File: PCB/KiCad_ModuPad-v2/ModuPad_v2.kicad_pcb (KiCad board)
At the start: 2 copper layers, 105 x 125 mm, 95 parts, among them J1 Conn_01x02, SW1 SW_Push, SW10 SW_Push, SW11 SW_Push, SW12 SW_Push, SW13 SW_Push, SW14 SW_Push, SW15 SW_Push, SW16 SW_Push, SW17 SW_Push, SW18 SW_Push, SW19 SW_Push, SW2 SW_Push, SW20 SW_Push, SW21 SW_Push, SW22 SW_Push, SW23 SW_Push, SW24 SW_Push, SW25 SW_Push, SW26_SPDT1 SW_SPDT, SW27_RST1 SW_Push_45deg, SW3 SW_Push, SW4 SW_Push, SW5 SW_Push, SW6 SW_Push, SW7 SW_Push, SW8 SW_Push, SW9 SW_Push

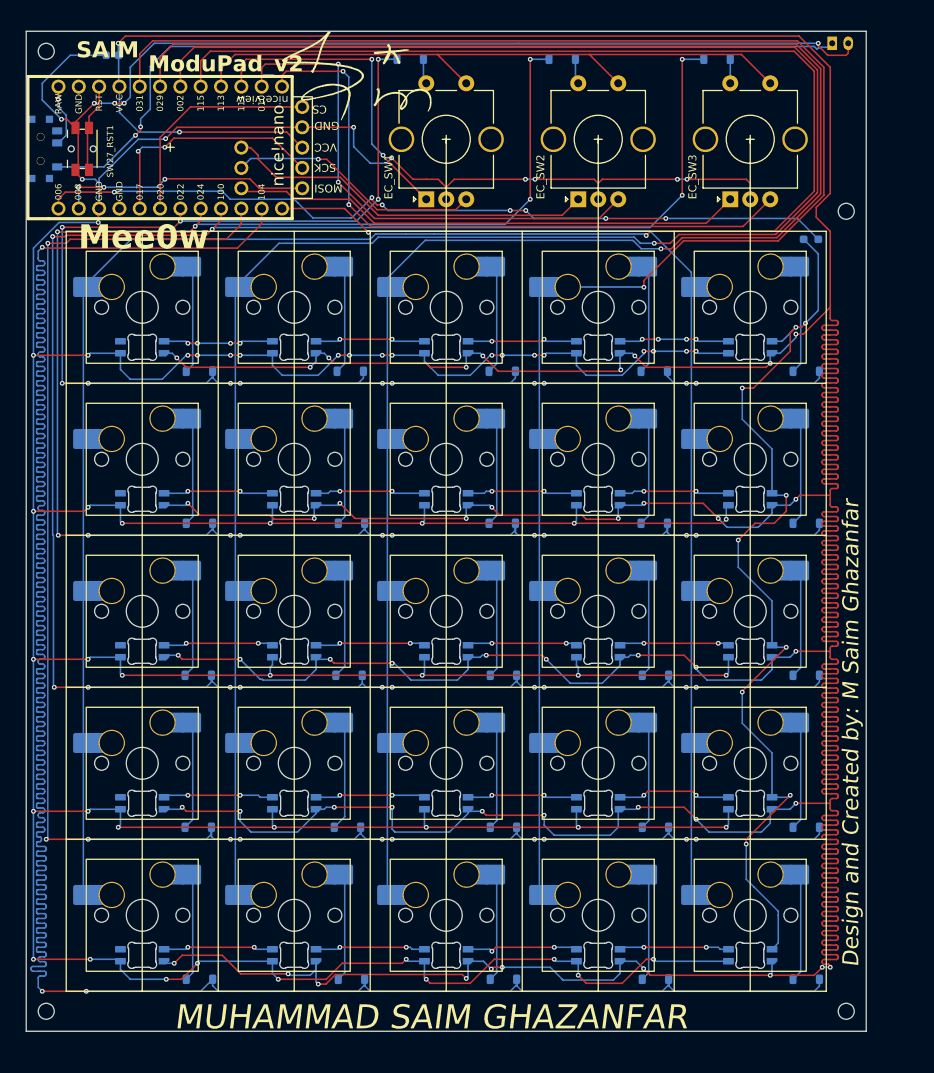
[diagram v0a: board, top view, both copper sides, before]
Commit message: Update BOM and PCB
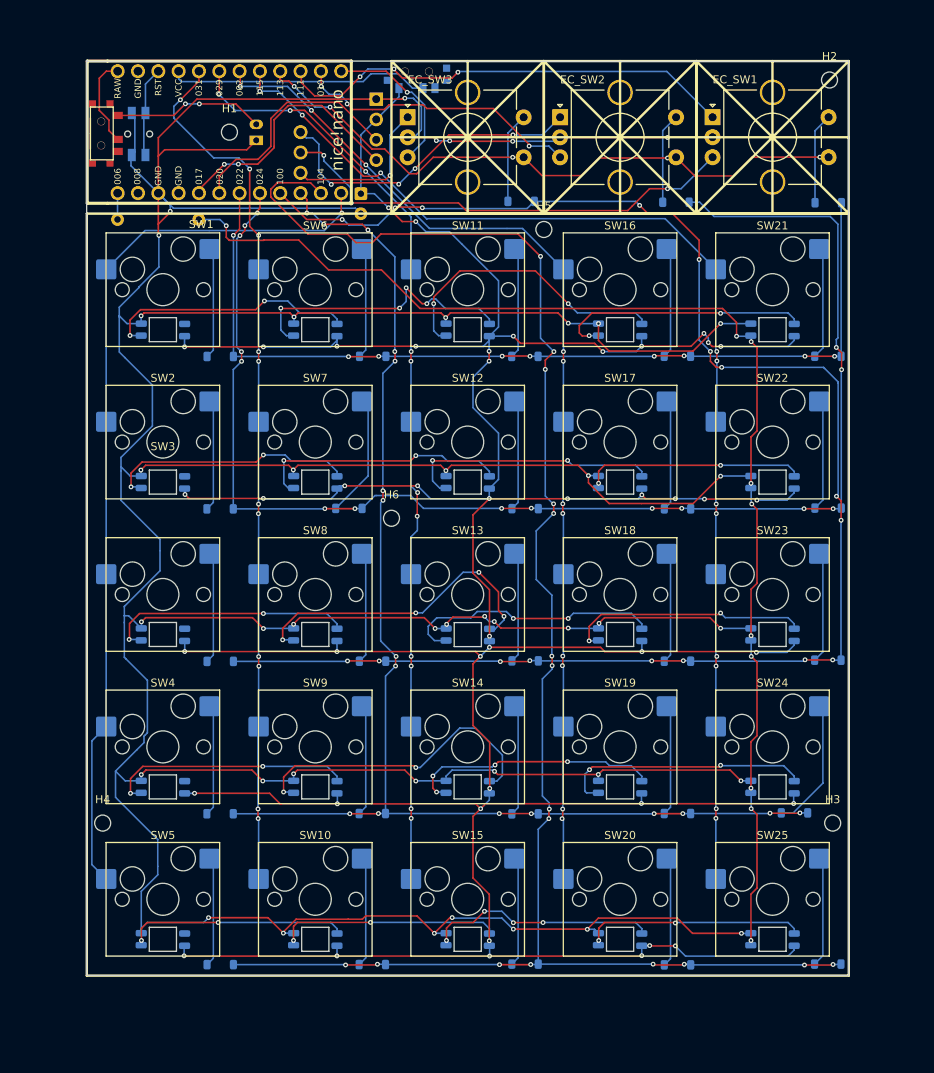
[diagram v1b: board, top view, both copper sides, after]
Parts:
- removed Display1: nice!view, nice!view:nice_view
- removed G*** (x2): LOGO, SAIM's_Signature-Silkscreen:SAIM_Signature_Silkscreen_20x18.4-mm
- removed G***: LOGO, Branding:Flag-orpheus-bw_Branding_HACK-CLUB
- removed REF** (x4): MountingHole_2mm, MountingHole:MountingHole_2mm
- removed SW26_SPDT1: SW_SPDT, Power-Switch-Battery:SPDT_C128955
- added BAT-Power-Switch_SPDT1: SW_SPDT, Power-Switch-Battery:SPDT_C128955, B.Cu at (59.4, 62.8)
- added H1: MountingHole, MountingHole:MountingHole_2mm, F.Cu at (75.4, 62.6)
- added H2: MountingHole, MountingHole:MountingHole_2mm, F.Cu at (150.4, 56.1)
- added H3: MountingHole, MountingHole:MountingHole_2mm, F.Cu at (150.8, 149.0)
- added H4: MountingHole, MountingHole:MountingHole_2mm, F.Cu at (59.6, 149.0)
- added H5: MountingHole, MountingHole:MountingHole_2mm, F.Cu at (114.7, 74.8)
- added H6: MountingHole, MountingHole:MountingHole_2mm, F.Cu at (95.7, 110.9)
- added J2: OLED_128x32, ScottoKeebs_Components:OLED_128x32, F.Cu at (95.3, 68.3)
- added LED-OLED-Power-Switch_SPDT2: SW_SPDT, Power-Switch-Battery:SPDT_C128955, F.Cu at (98.8, 55.0)
- C1: footprint Capacitor_SMD:C_0603_1608Metric -> Capacitor_THT:CP_Radial_D6.3mm_P2.50mm
- D_1, D_10, D_11, D_12, D_13, D_14, D_15, D_16, D_17, D_18, D_19, D_2, D_20, D_21, D_22, D_23, D_24, D_25, D_26, D_27, D_28, D_3, D_4, D_5, D_6, D_7, D_8, D_9: footprint Diode_SMD:D_SOD-123 -> ScottoKeebs_Components:Diode_SOD-123
- LED_1, LED_10, LED_11, LED_12, LED_13, LED_14, LED_15, LED_16, LED_17, LED_18, LED_19, LED_2, LED_20, LED_21, LED_22, LED_23, LED_24, LED_25, LED_3, LED_4, LED_5, LED_6, LED_7, LED_8, LED_9: footprint SK6812MINI-E:SK6812MINI-E -> SK6812MINI-E:LED_SK6812MINI; moved to F.Cu
- R1: footprint Resistor_SMD:R_0603_1608Metric_Pad0.98x0.95mm_HandSolder -> Resistor_THT:R_Axial_DIN0207_L6.3mm_D2.5mm_P10.16mm_Horizontal
- SW1, SW10, SW11, SW12, SW13, SW14, SW15, SW16, SW17, SW18, SW19, SW2, SW20, SW21, SW22, SW23, SW24, SW25, SW3, SW4, SW5, SW6, SW7, SW8, SW9: footprint MX-Style-Cherry-Switches-with-Kilah-HotSwap-Socket:SW_MX_HS_CPG151101S11_1u -> ScottoKeebs_Hotswap:Hotswap_MX_1.00u; moved to F.Cu
- SW27_RST1: moved to B.Cu
- moved R1 86.7 mm to (61.4, 73.5), turned to 0 degrees
- moved SW21 78.8 mm to (143.3, 82.3), turned to 0 degrees
- moved SW22 78.8 mm to (143.3, 101.3), turned to 0 degrees
- moved SW23 78.8 mm to (143.3, 120.4), turned to 0 degrees
- moved SW24 78.8 mm to (143.3, 139.4), turned to 0 degrees
- moved SW25 78.8 mm to (143.3, 158.5), turned to 0 degrees
- moved D_23 78.7 mm to (150.2, 128.6)
- moved D_22 78.6 mm to (150.2, 109.6)
- moved D_21 78.6 mm to (150.2, 90.6)
- moved D_25 78.6 mm to (150.2, 166.6)
- moved D_24 74.6 mm to (146.0, 147.7)
- moved J1 73.8 mm to (78.8, 62.6), turned to 90 degrees
- moved SW1 73.5 mm to (67.1, 82.3), turned to 0 degrees
- moved SW2 73.5 mm to (67.1, 101.3), turned to 0 degrees
- moved SW3 73.5 mm to (67.1, 120.4), turned to 0 degrees
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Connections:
- net MCU-RST renamed RST
- C1 pad 1: VCC -> LED_DISP_PWR
- J1 pad 1: BAT+ -> GND
- J1 pad 2: GND -> BAT+
- LED_1 pad 4: VCC -> LED_DISP_PWR
- LED_10 pad 4: VCC -> LED_DISP_PWR
- LED_11 pad 4: VCC -> LED_DISP_PWR
- LED_12 pad 4: VCC -> LED_DISP_PWR
- LED_13 pad 4: VCC -> LED_DISP_PWR
- LED_14 pad 4: VCC -> LED_DISP_PWR
- LED_15 pad 4: VCC -> LED_DISP_PWR
- LED_16 pad 4: VCC -> LED_DISP_PWR
- LED_17 pad 4: VCC -> LED_DISP_PWR
- LED_18 pad 4: VCC -> LED_DISP_PWR
- LED_19 pad 4: VCC -> LED_DISP_PWR
- LED_2 pad 4: VCC -> LED_DISP_PWR
- LED_20 pad 4: VCC -> LED_DISP_PWR
- LED_21 pad 4: VCC -> LED_DISP_PWR
- LED_22 pad 4: VCC -> LED_DISP_PWR
- LED_23 pad 4: VCC -> LED_DISP_PWR
- LED_24 pad 4: VCC -> LED_DISP_PWR
- LED_25 pad 4: VCC -> LED_DISP_PWR
- LED_3 pad 4: VCC -> LED_DISP_PWR
- LED_4 pad 4: VCC -> LED_DISP_PWR
- LED_5 pad 4: VCC -> LED_DISP_PWR
- LED_6 pad 4: VCC -> LED_DISP_PWR
- LED_7 pad 4: VCC -> LED_DISP_PWR
- LED_8 pad 4: VCC -> LED_DISP_PWR
- LED_9 pad 4: VCC -> LED_DISP_PWR
- MCU1 pad 2: nice!view_MOSI -> unconnected-(MCU1-RX1/P0.08-Pad2)
- MCU1 pad 5: nice!view_SCK -> SDA
- MCU1 pad 6: nice!view_CS -> SCL
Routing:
- net VCC: track 943.6 -> 32.8 mm, vias 48 -> 0
- net LED_DISP_PWR: track 0.00 -> 539.2 mm, vias 0 -> 44
- net ROW 4: track 359.4 -> 215.2 mm, vias 3 -> 17
- net GND: track 827.3 -> 683.6 mm, vias 63 -> 42
- net COL 3: track 254.3 -> 128.3 mm, vias 1 -> 11
- net COL 2: track 240.3 -> 116.8 mm, vias 1 -> 11
- net COL 4: track 268.9 -> 145.6 mm, vias 1 -> 11
- net COL 1: track 222.8 -> 108.6 mm, vias 1 -> 11
- net LED: track 101.3 -> 3.31 mm, vias 7 -> 0
- net BAT+: track 107.5 -> 19.0 mm
- net ROW 0: track 185.2 -> 116.0 mm, vias 14 -> 9
- net ROW 2: track 264.3 -> 201.5 mm, vias 14 -> 17
- net EC_03_RB: track 81.4 -> 19.6 mm, vias 2 -> 1
- net ROW 1: track 226.1 -> 174.4 mm, vias 14 -> 15
- net ROW 3: track 208.3 -> 159.7 mm, vias 11 -> 17
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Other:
- board size 105 x 125 mm -> 95.3 x 114.3 mm
- board text removed: "Design and Created by: M Saim Ghazanfar"
- board text removed: "MUHAMMAD SAIM GHAZANFAR"
- board text removed: "Mee0w"
- board text removed: "ModuPad_v2"
- board text removed: "SAIM"

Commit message: Update
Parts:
- added G***: LOGO, Branding:Flag-Standalone-bw_Branding_HACK-CLUB, F.Cu at (138.8, 73.1)
- added G***: LOGO, SAIM's_Signature-Silkscreen:SAIM_Signature_Silkscreen_20x18.4-mm, B.Cu at (141.9, 60.6)
- added G***: LOGO, Branding:Icon-Rounded-Original_Branding_S-Letter, B.Cu at (104.9, 63.2)
- added G***: LOGO, Branding:Flag-Standalone-bw_Branding_HACK-CLUB, B.Cu at (132.4, 73.5)
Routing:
- added copper zone on B.Cu, net (none)
- added copper zone on F.Cu, net (none)
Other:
- board text added: "Made With Love BY SAIM"
